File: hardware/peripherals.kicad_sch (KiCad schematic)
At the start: 32 parts, among them J6 PCM12SMTR, J7 USB_C_Receptacle_USB2.0_14P, J8 BM03B-SRSS-TB, Q4 2N7002, SW1 SW_Push, U3 74AHCT1G125, U4 DS3231MZ, U5 USBLC6-2SC6, U6 74AHCT1G32

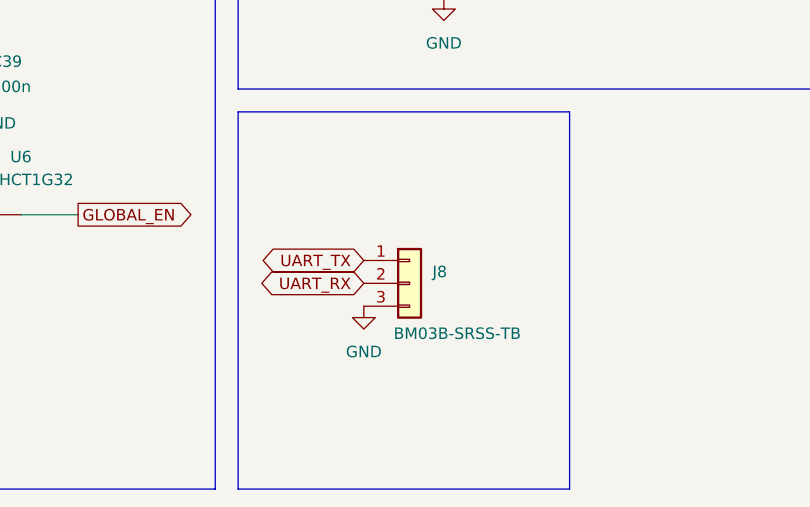
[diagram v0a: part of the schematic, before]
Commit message: fix: J8 UART pinout now GND-TX-RX (standard convention)
Pin 1: GND, Pin 2: TX, Pin 3: RX
DRC clean, 0 violations.
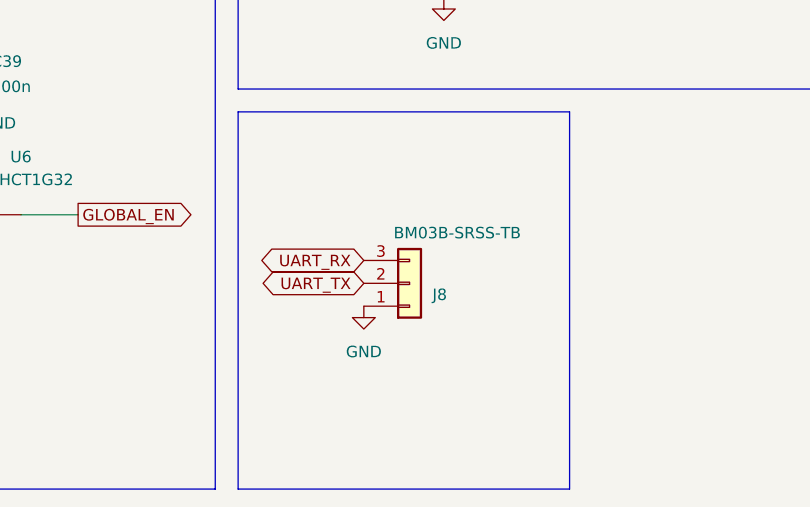
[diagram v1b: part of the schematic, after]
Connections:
- net GND: now also J8.1 (Pin_1); no longer J8.3 (Pin_3)
- net UART_RX: now also J8.3 (Pin_3); no longer J8.2 (Pin_2)
- net UART_TX: now also J8.2 (Pin_2); no longer J8.1 (Pin_1)
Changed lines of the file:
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@@
 		)
 	)
-	(global_label "UART_TX"
-		(shape bidirectional)
-		(at 143.51 170.18 180)
-		(fields_autoplaced yes)
-		(effects
-			(font
-				(size 1.27 1.27)
-			)
-			(justify right)
-		)
-		(property "Intersheetrefs" "${INTERSHEET_REFS}"
-			(at 131.6121 170.18 0)
-			(hide yes)
-			(show_name no)
-			(do_not_autoplace no)
-			(effects
-				(font
-					(size 1.27 1.27)
-				)
-				(justify right)
-			)
-		)
-	)
 	(global_label "SCL1"
 		(shape bidirectional)
@@
 		)
 	)
-	(global_label "UART_RX"
+	(global_label "UART_TX"
 		(shape bidirectional)
 		(at 143.51 172.72 180)
@@
 		)
 		(property "Intersheetrefs" "${INTERSHEET_REFS}"
-			(at 131.3097 172.72 0)
+			(at 131.6121 172.72 0)
 			(hide yes)
 			(show_name no)
@@
 		)
 	)
+	(global_label "UART_RX"
+		(shape bidirectional)
+		(at 143.51 170.18 180)
+		(fields_autoplaced yes)
+		(effects
+			(font
+				(size 1.27 1.27)
+			)
+			(justify right)
+		)
+		(property "Intersheetrefs" "${INTERSHEET_REFS}"
+			(at 131.3097 170.18 0)
+			(hide yes)
+			(show_name no)
+			(do_not_autoplace no)
+			(effects
+				(font
+					(size 1.27 1.27)
+				)
+				(justify right)
+			)
+		)
+	)
 	(global_label "nLED_PWR"
 		(shape bidirectional)
@@
 		(lib_id "Connector_Generic:Conn_01x03")
 		(at 148.59 172.72 0)
+		(mirror x)
 		(unit 1)
 		(body_style 1)
@@
 		(dnp no)
 		(property "Reference" "J8"
-			(at 151.13 171.4499 0)
+			(at 151.13 173.9901 0)
 			(show_name no)
 			(do_not_autoplace no)
@@
 		)
 		(property "Value" "BM03B-SRSS-TB"
-			(at 146.812 178.308 0)
+			(at 146.812 167.132 0)
 			(show_name no)
 			(do_not_autoplace no)
